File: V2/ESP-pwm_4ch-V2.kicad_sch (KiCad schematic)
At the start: 32 parts, among them J1 12VDC, J2 OUT1, J3 OUT2, J4 OUT3, J5 OUT4, Q1 IRLB8721PBF, Q2 IRLB8721PBF, Q3 IRLB8721PBF, Q4 IRLB8721PBF, U1 L78M05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

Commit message: work in progress
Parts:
- C5, C7: JLCPCB BOM 0 -> 1; LCSC Part (none) -> C7176; Mfr PN TAJA105K035TNJ -> TAJA105K035RNJ; Vendor Mouser -> JLCPCB; Vendor PN 581-TAJA105K035TNJ -> C7176
- U4, U5: JLCPCB BOM 0 -> 1; LCSC Part (none) -> C49058; Vendor Mouser -> JLCPCB; Vendor PN 942-IR4427STRPBFr -> C49058
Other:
- note added: "ESP32 DATA PIN D15 (13) -> OUT 1 DATA PIN D16 (14) -> OUT 2 DATA PIN D32 (15) -> OUT 3 DATA PIN D33 (16) -> OUT 4"
- note added: "ESP8266 DATA PIN D6 (5) -> OUT 1 DATA PIN D5 (4) -> OUT 2 DATA PIN D2 (13) -> OUT 3 DATA PIN D1 (14) -> OUT 4"
- moved on the sheet: J2, J4, Q1, Q3, R4, R6

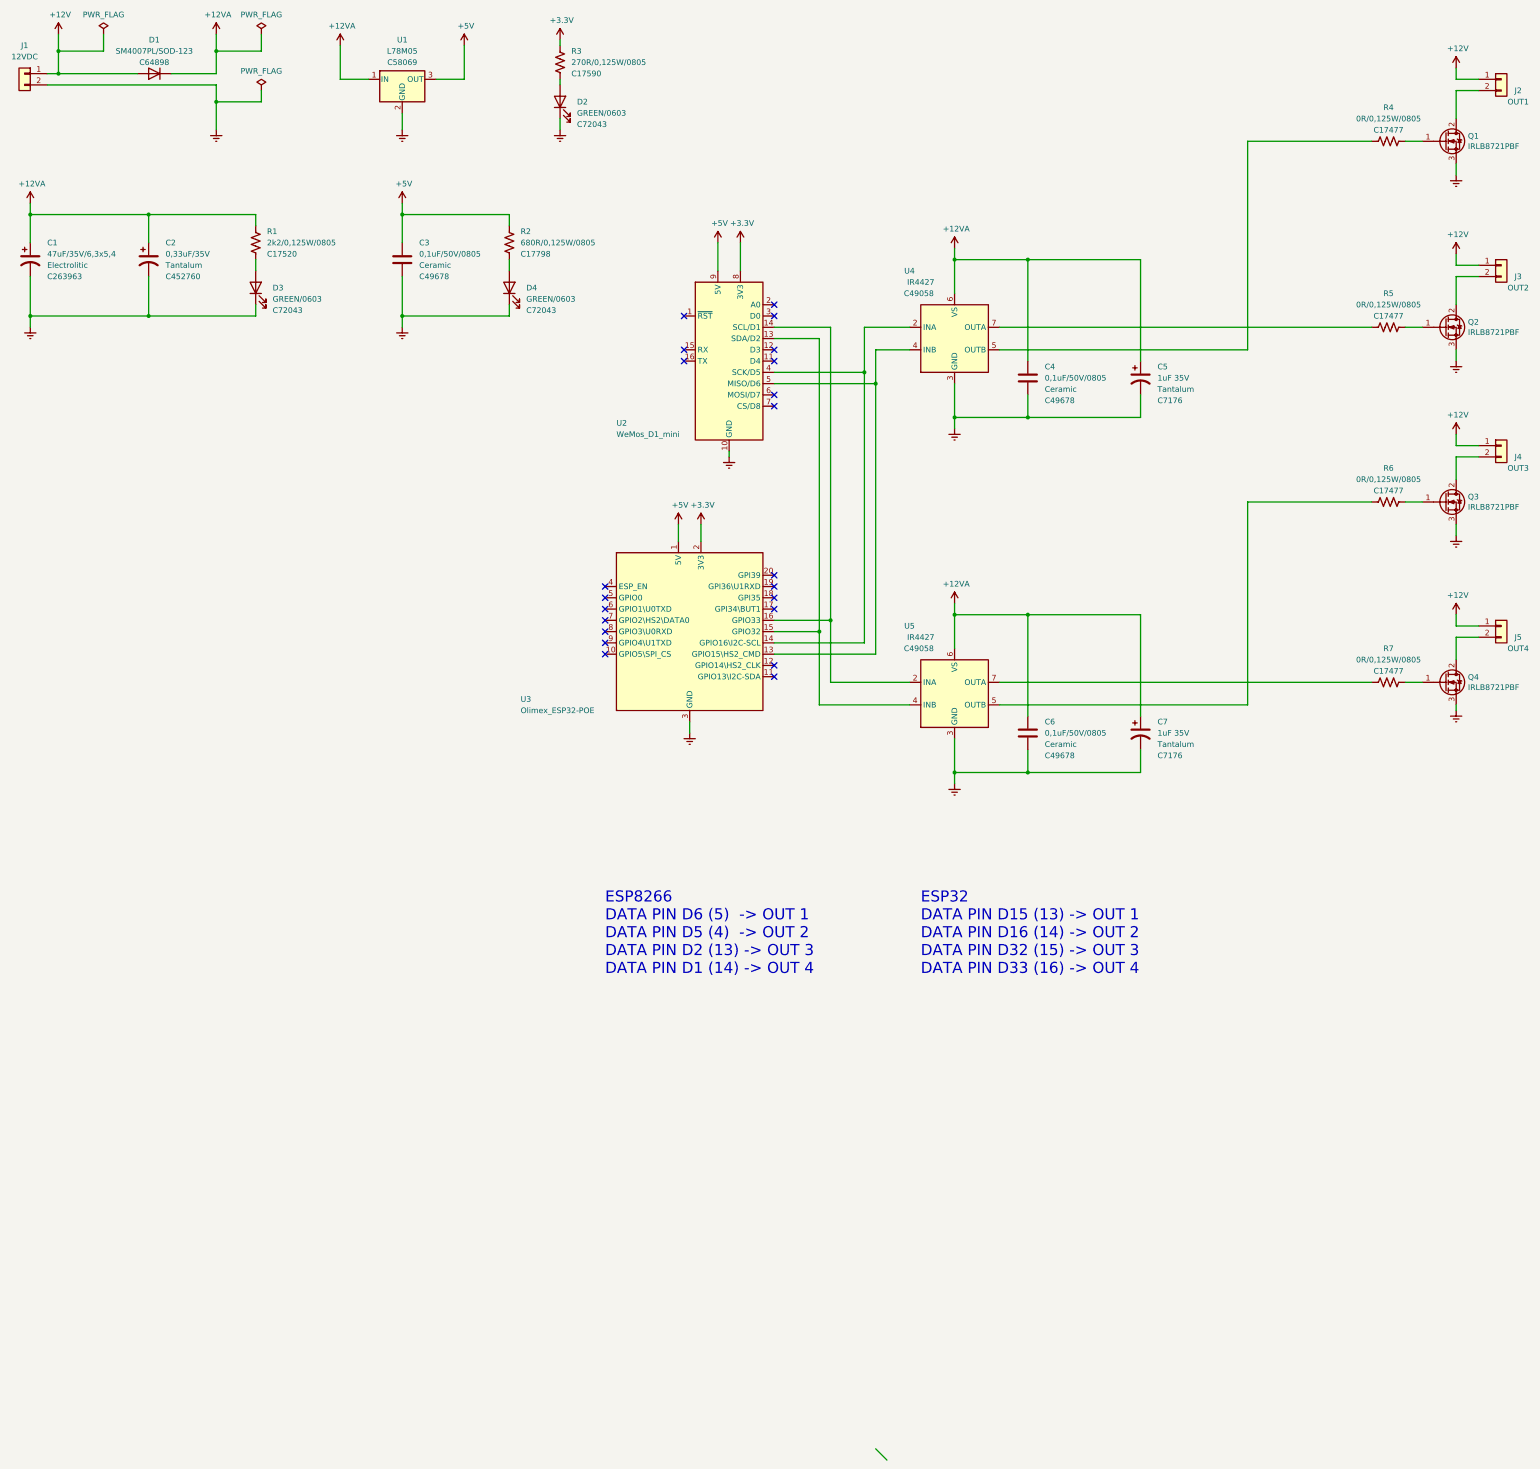
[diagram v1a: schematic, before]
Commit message: Gate resistor from 0R to 22R
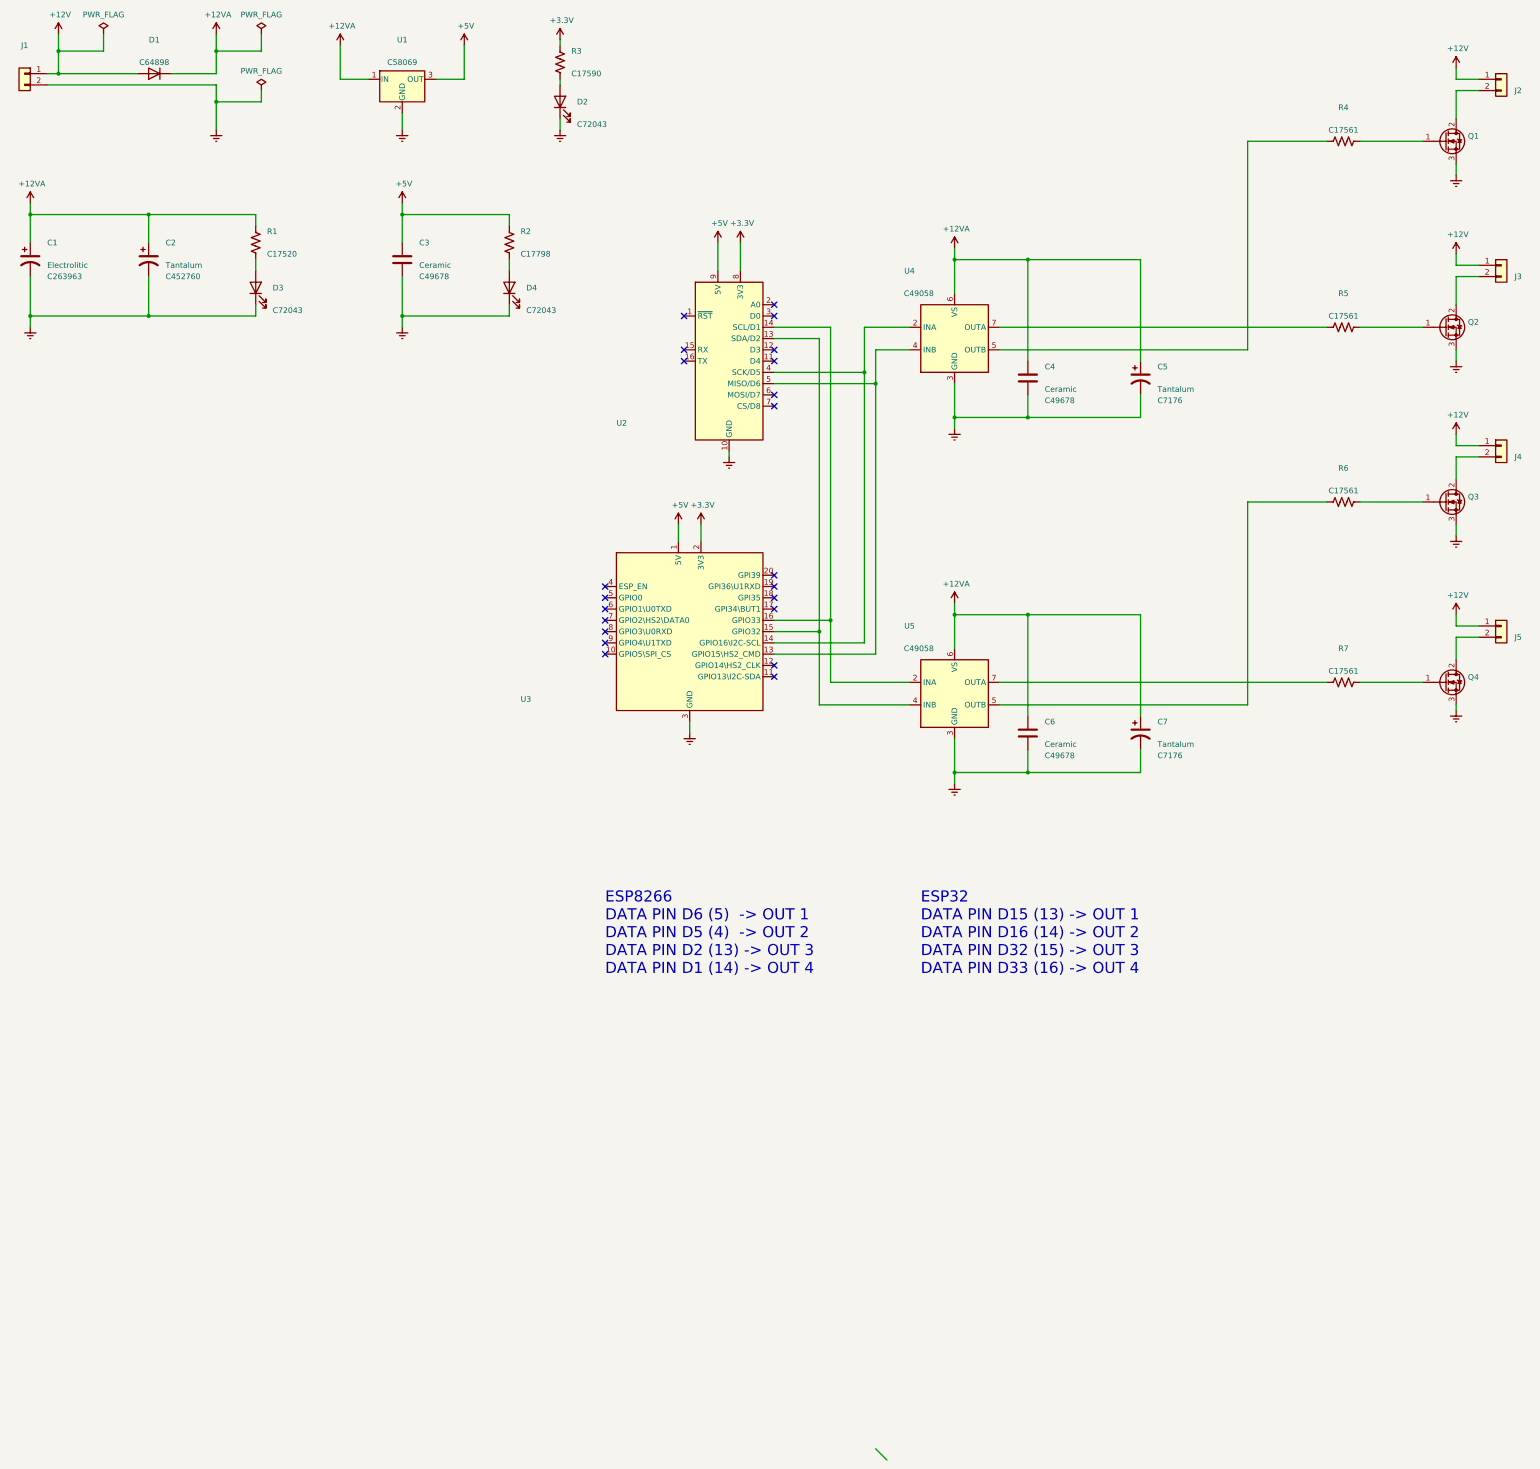
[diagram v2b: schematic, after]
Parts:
- C1: value 47uF/35V/6,3x5,4 -> (none); footprint Tales:CP_Elec_6.3x5.4 -> (none)
- C2: value 0,33uF/35V -> (none); footprint Tales:CP_EIA-3216-18_Kemet-A_Pad1.58x1.35mm_HandSolder -> (none)
- C3, C4, C6: value 0,1uF/50V/0805 -> (none); footprint Tales:C_0805_2012Metric -> (none)
- C5, C7: value 1uF 35V -> (none); footprint Tales:CP_EIA-3216-18_Kemet-A_Pad1.58x1.35mm_HandSolder -> (none)
- D1: value SM4007PL/SOD-123 -> (none); footprint Tales:D_SOD-123 -> (none)
- D2, D3, D4: value GREEN/0603 -> (none); footprint Tales:LED_0603_1608Metric -> (none)
- J1: value 12VDC -> (none); footprint Tales:TerminalBlock_Phoenix_MKDS-3-2-5.08_1x02_P5.08mm_Horizontal -> (none)
- J2: value OUT1 -> (none); footprint Tales:TerminalBlock_Phoenix_MKDS-3-2-5.08_1x02_P5.08mm_Horizontal -> (none)
- J3: value OUT2 -> (none); footprint Tales:TerminalBlock_Phoenix_MKDS-3-2-5.08_1x02_P5.08mm_Horizontal -> (none)
- J4: value OUT3 -> (none); footprint Tales:TerminalBlock_Phoenix_MKDS-3-2-5.08_1x02_P5.08mm_Horizontal -> (none)
- J5: value OUT4 -> (none); footprint Tales:TerminalBlock_Phoenix_MKDS-3-2-5.08_1x02_P5.08mm_Horizontal -> (none)
- Q1, Q2, Q3, Q4: value IRLB8721PBF -> (none); footprint Package_TO_SOT_THT:TO-220-3_Vertical -> (none)
- R1: value 2k2/0,125W/0805 -> (none); footprint Tales:R_0805_2012Metric -> (none)
- R2: value 680R/0,125W/0805 -> (none); footprint Tales:R_0805_2012Metric -> (none)
- R3: value 270R/0,125W/0805 -> (none); footprint Tales:R_0805_2012Metric -> (none)
- R4, R5, R6, R7: value 0R/0,125W/0805 -> (none); footprint Tales:R_0805_2012Metric -> (none); LCSC Part C17477 -> C17561; Mfr PN 0805W8F0000T5E -> 0805W8F220JT5E; Vendor PN C17477 -> C17561
- U1: value L78M05 -> (none); footprint Tales:TO-252-2 -> (none)
- U2: value WeMos_D1_mini -> (none); footprint Tales:WEMOS_D1_mini_light_pads -> (none)
- U3: value Olimex_ESP32-POE -> (none); footprint Tales:Olimex_ESP32-POE_Pads -> (none)
- U4, U5: value IR4427 -> (none); footprint Package_SO:SOIC-8_3.9x4.9mm_P1.27mm -> (none)
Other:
- moved on the sheet: R4, R5, R6, R7

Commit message: Reset pulled up to +3.3V
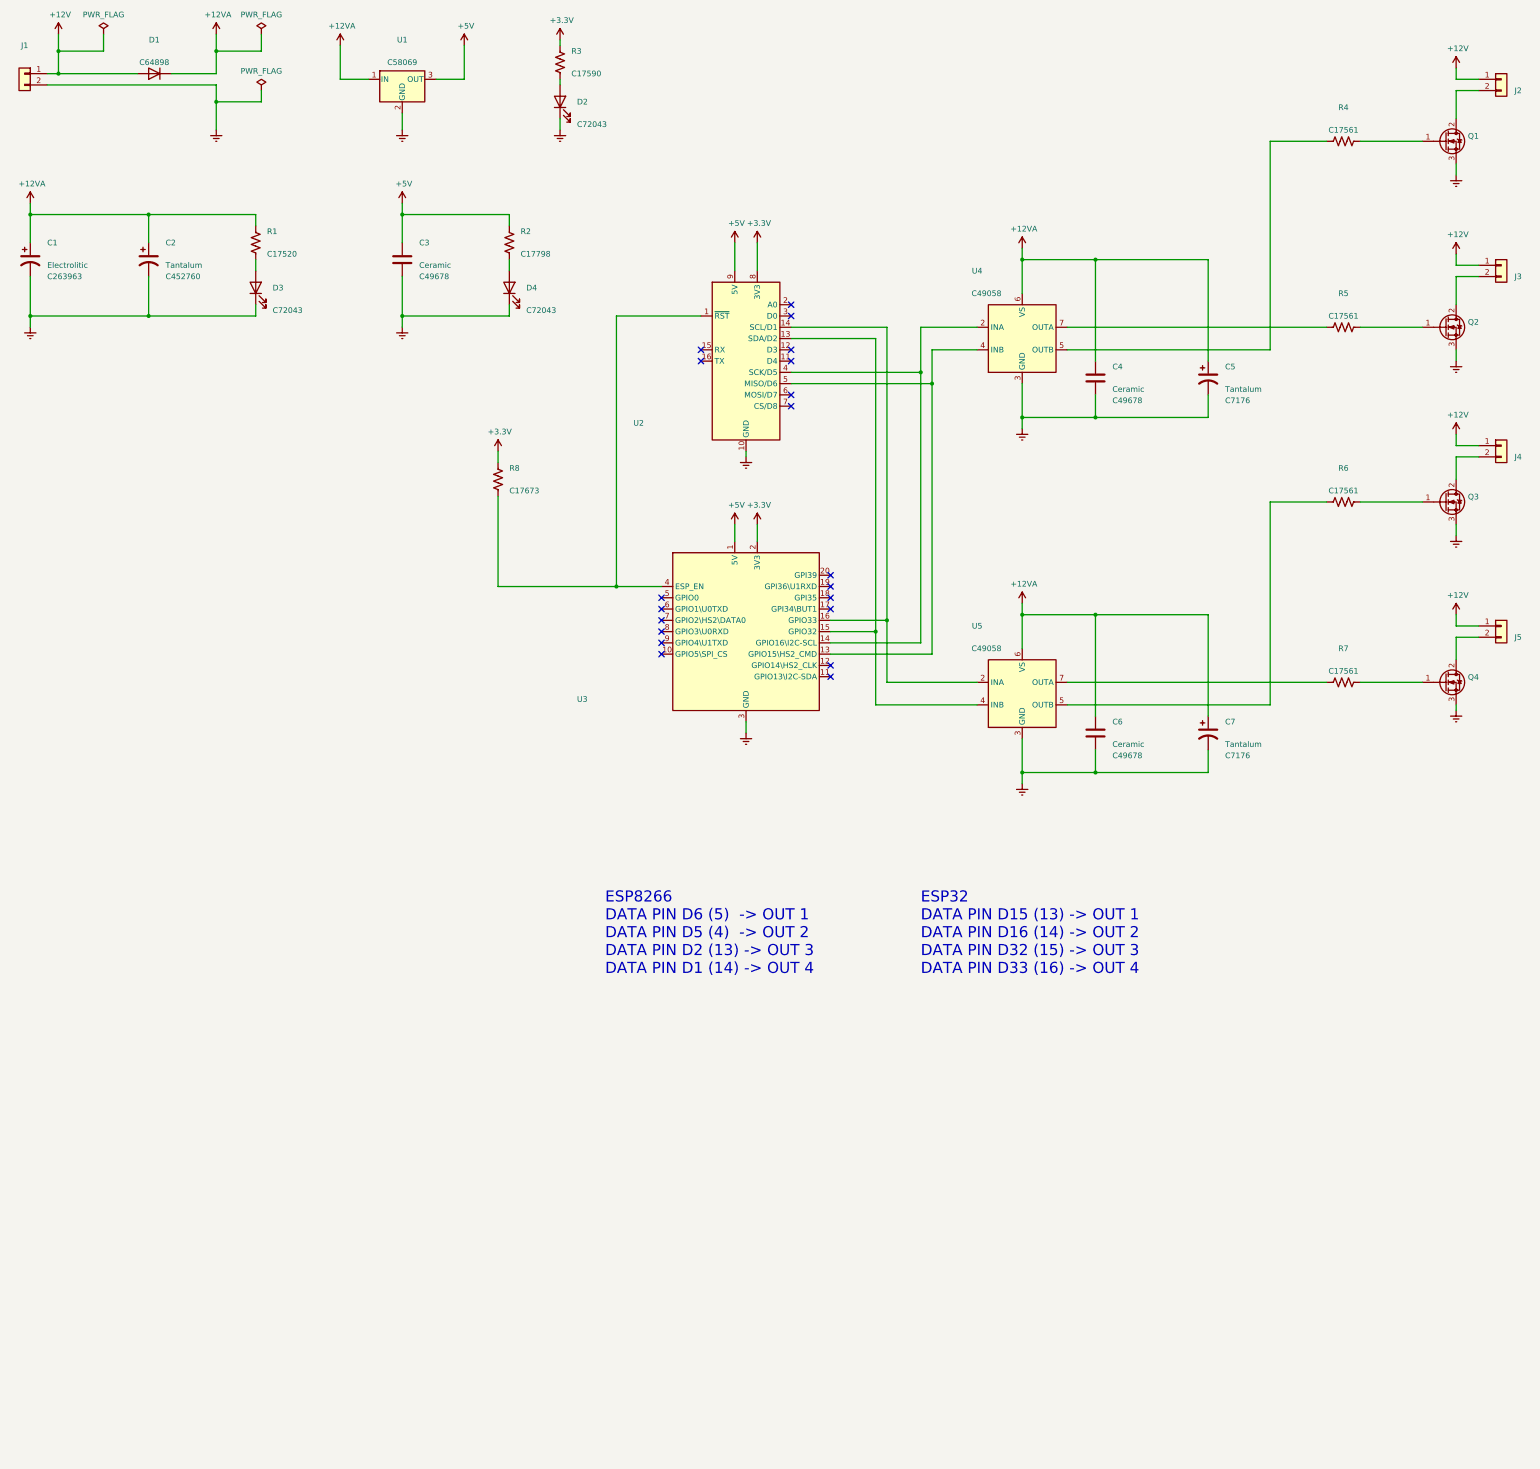
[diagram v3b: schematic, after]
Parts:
- added R8: (no value), symbol Device:R_US
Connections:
- net +3V3: now also R8.1
- net at U3.4 (ESP_EN): now also U2.1 (~{RST}), R8.2
- no-connect marks 22 -> 20
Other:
- moved on the sheet: C4, C5, C6, C7, U2, U3, U4, U5
